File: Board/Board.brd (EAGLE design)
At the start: 72 x 50 mm, 19 parts

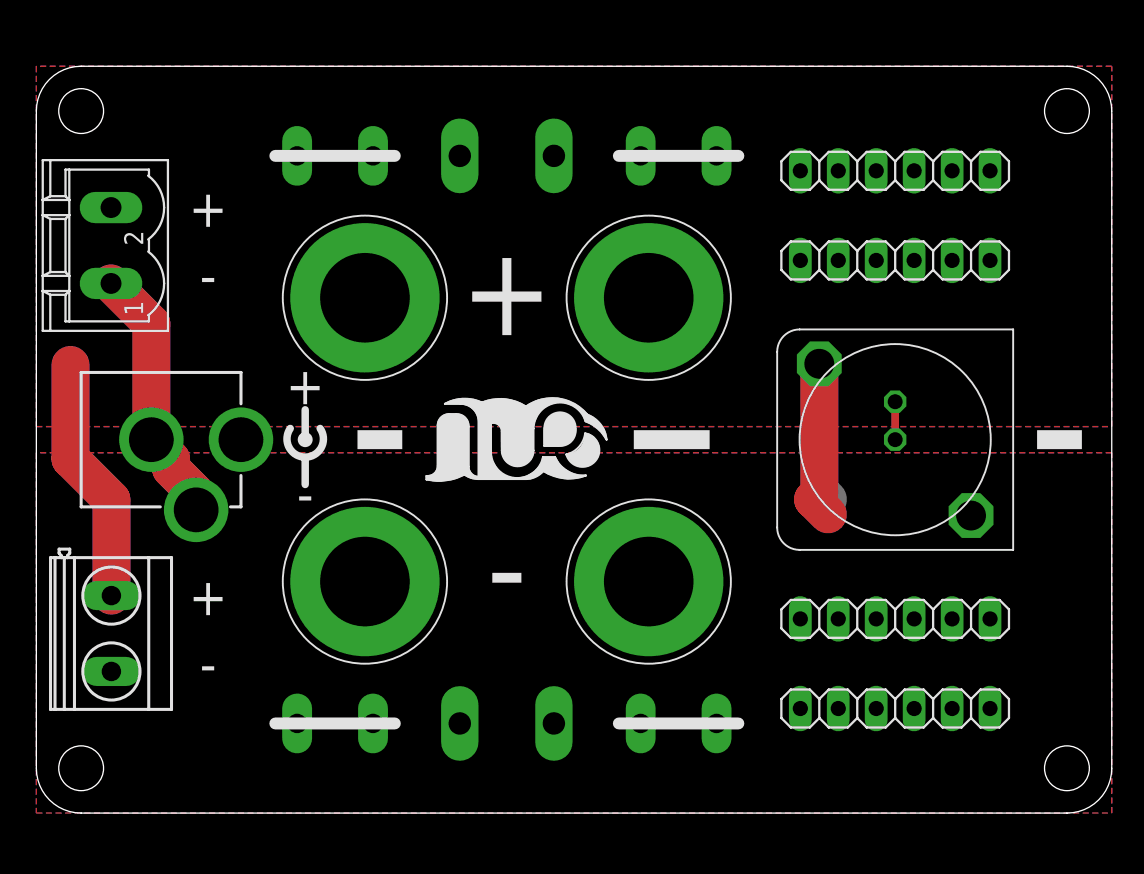
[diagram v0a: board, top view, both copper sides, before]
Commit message: moved BNC to center for better access to lower profile connectors
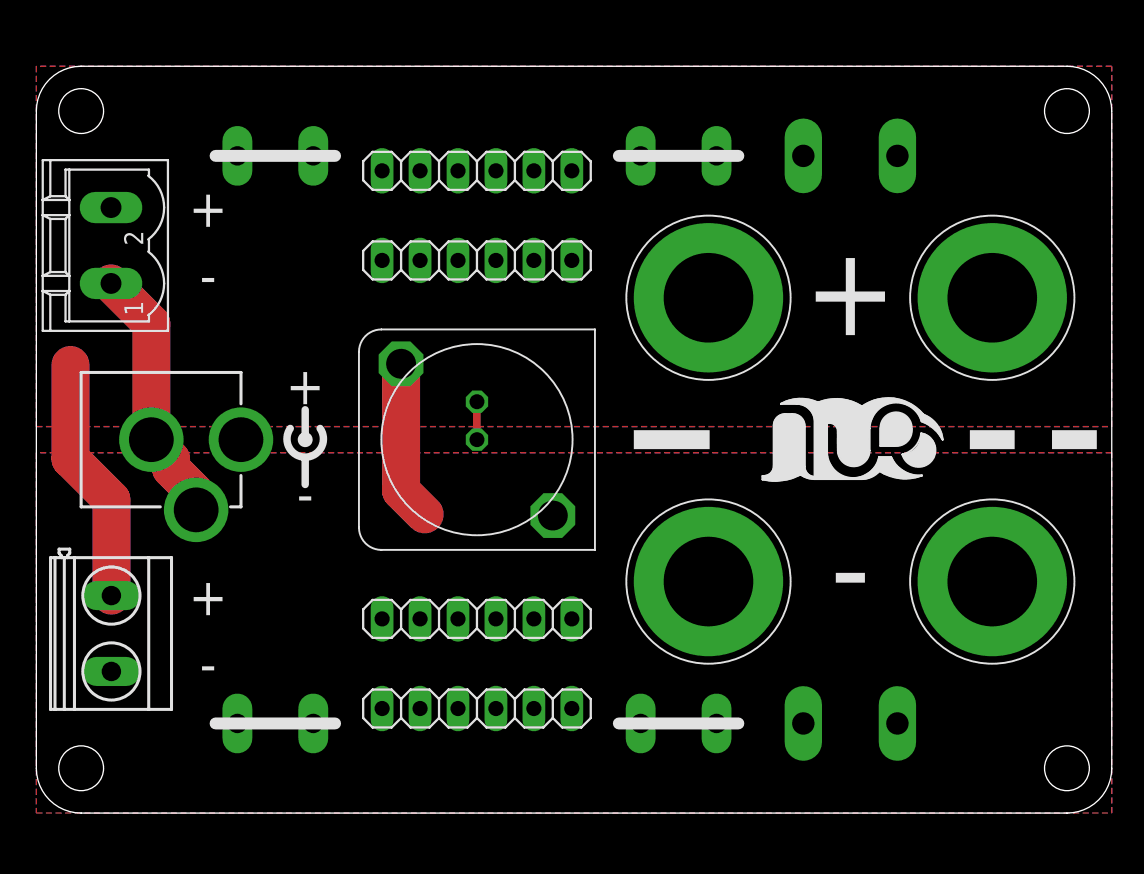
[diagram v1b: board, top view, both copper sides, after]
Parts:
- moved U$5 28.0 mm to (29.5, 25.0)
- moved U$6 28.0 mm to (29.5, 7.00)
- moved U$7 28.0 mm to (29.5, 43.0)
- moved U$8 28.0 mm to (29.5, 13.0)
- moved U$9 28.0 mm to (29.5, 37.0)
- moved U$18 27.0 mm to (16.0, 6.00), turned to 180 degrees
- moved U$19 27.0 mm to (16.0, 44.0), turned to 180 degrees
- moved U$1 23.0 mm to (64.0, 15.5), turned to 180 degrees
- moved U$14 23.0 mm to (43.0, 6.00), turned to 180 degrees
- moved U$15 23.0 mm to (43.0, 44.0), turned to 180 degrees
- moved U$16 23.0 mm to (54.5, 44.0)
- moved U$17 23.0 mm to (54.5, 6.00)
- moved U$2 23.0 mm to (45.0, 34.5), turned to 180 degrees
- moved U$3 23.0 mm to (45.0, 15.5), turned to 180 degrees
- moved U$4 23.0 mm to (64.0, 34.5), turned to 180 degrees
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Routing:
- net -: track 55.0 -> 56.5 mm

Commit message: implemented various suggestions from the forum post
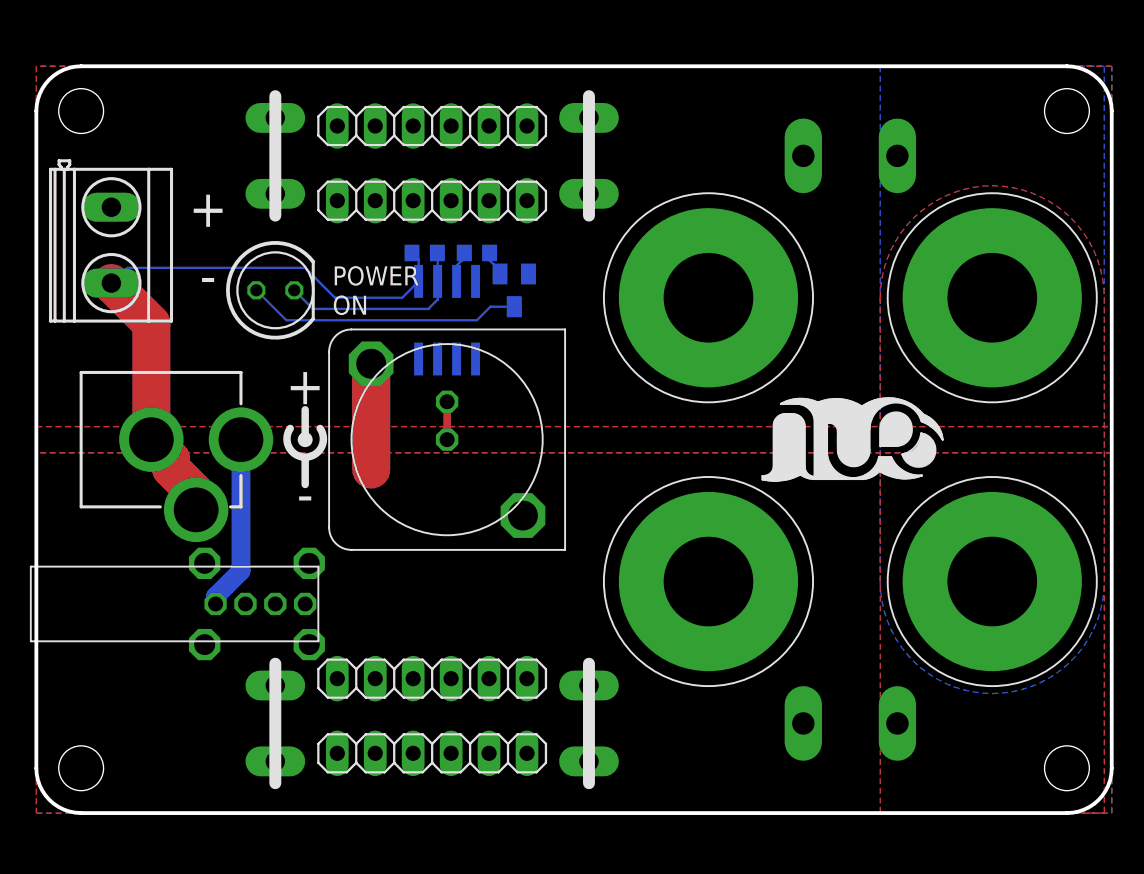
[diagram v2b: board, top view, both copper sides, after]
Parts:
- removed U$11: TERMINAL-BLOCK-2PLUG-IN, AdapterBoard:MSTBV2
- added IC1: LM334, linear:SO08
- added POWER: (no value), led:LED5MM
- added R1: 100, rcl:R0603
- added R2: 3R3, rcl:R0603
- added T1: BC807, transistor:SOT23-BEC
- added U$20: (no value), SparkFun-Aesthetics:OSHW-LOGO-L
- added U$21: USB, AdapterBoard:ECON-USBBUVA
- U$1, U$3: value 6MM-BANANA-PLUG -> 6MM-BANANA-PLUGSCREW-BLACK; device AdapterBoard:6MM-BANANA-MOUNT -> AdapterBoard:6MM-TERMINAL-POST-BLACK
- U$2, U$4: value 6MM-BANANA-PLUG -> 6MM-BANANA-PLUGSCREW-RED; device AdapterBoard:6MM-BANANA-MOUNT -> AdapterBoard:6MM-TERMINAL-POST-RED
- moved U$10 26.0 mm to (5.00, 38.0)
- moved U$1 19.0 mm to (64.0, 34.5)
- moved U$4 19.0 mm to (64.0, 15.5)
- moved U$14 6.00 mm to (37.0, 6.00), turned to 270 degrees
- moved U$15 6.00 mm to (37.0, 44.0), turned to 270 degrees
- moved U$8 5.00 mm to (26.5, 9.00)
- moved U$9 5.00 mm to (26.5, 41.0)
- moved U$6 4.24 mm to (26.5, 4.00)
- moved U$7 4.24 mm to (26.5, 46.0)
- moved U$5 2.00 mm to (27.5, 25.0)
- turned U$18 to 90 degrees
- turned U$19 to 90 degrees
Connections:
- removed net +: U$10.1, U$11.2, U$12.PWR, U$15.P$1, U$15.P$2, U$16.P$1, U$16.P$2, U$19.P$1, U$19.P$2, U$2.P$1, U$4.P$1, U$5.CONDUCTOR1, U$5.CONDUCTOR2, U$7.1, U$7.2, U$7.3, U$7.4, U$7.5, U$7.6, U$9.1, U$9.2, U$9.3, U$9.4, U$9.5, U$9.6
- removed net -: U$1.P$1, U$10.2, U$11.1, U$12.GND, U$12.GNDBREAK, U$14.P$1, U$14.P$2, U$17.P$1, U$17.P$2, U$18.P$1, U$18.P$2, U$3.P$1, U$5.SHIELD1, U$5.SHIELD2, U$6.1, U$6.2, U$6.3, U$6.4, U$6.5, U$6.6, U$8.1, U$8.2, U$8.3, U$8.4, U$8.5, U$8.6
- new net N$1: IC1.2, POWER.K, R2.2
- new net N$2: R1.2, T1.B
- new net N$3: IC1.3, R1.1
- new net N$4: POWER.A, T1.C
- new net V+: T1.E, U$10.1, U$12.PWR, U$15.P$1, U$15.P$2, U$16.P$1, U$16.P$2, U$19.P$1, U$19.P$2, U$2.P$1, U$21.V+, U$4.P$1, U$5.CONDUCTOR1, U$5.CONDUCTOR2, U$7.1, U$7.2, U$7.3, U$7.4, U$7.5, U$7.6, U$9.1, U$9.2, U$9.3, U$9.4, U$9.5, U$9.6
- new net V-: IC1.1, R2.1, U$1.P$1, U$10.2, U$12.GND, U$12.GNDBREAK, U$14.P$1, U$14.P$2, U$17.P$1, U$17.P$2, U$18.P$1, U$18.P$2, U$21.S1, U$21.S2, U$21.S3, U$21.S4, U$21.V-, U$3.P$1, U$5.SHIELD1, U$5.SHIELD2, U$6.1, U$6.2, U$6.3, U$6.4, U$6.5, U$6.6, U$8.1, U$8.2, U$8.3, U$8.4, U$8.5, U$8.6
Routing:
- net V-: track 0.00 -> 73.6 mm
- net -: track 56.5 -> 0.00 mm
- net +: track 35.7 -> 0.00 mm
- net N$4: track 0.00 -> 18.5 mm
- net V+: track 0.00 -> 14.2 mm
- net N$1: track 0.00 -> 13.5 mm
- net N$3: track 0.00 -> 2.11 mm
- net N$2: track 0.00 -> 1.69 mm
- added copper zone on layer 1, net V+
- added copper zone on layer 16, net V+
- added copper zone on layer 1, net V-
- added copper zone on layer 16, net V-
- removed copper zone on layer 1, net +
- removed copper zone on layer 16, net +
- removed copper zone on layer 1, net -
- removed copper zone on layer 16, net -
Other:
- board text added: "ON"
- board text added: "https://github.com/dangrie158/AdapterBox"

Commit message: fixed BNC pinout
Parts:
- removed U$20: (no value), SparkFun-Aesthetics:OSHW-LOGO-L
- turned U$5 to 90 degrees
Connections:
- net V+: no longer U$5.CONDUCTOR2
- net V-: now also U$5.CONDUCTOR2
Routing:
- net V+: track 14.2 -> 51.2 mm
- net V-: track 73.6 -> 94.5 mm

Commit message: updated BNC footprint
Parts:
- T1: device transistor:SOT23-BEC -> DC_LOAD_AU:SOT23-BEC
- U$5: value BNC-VTE-1-1337541-0 -> BNC-V; device AdapterBoard:BNC-V -> AdapterBoard:TE-5-1634503-1
- U$6, U$7: value PINHD-6 -> (none); device AdapterBoard:1X06 -> SparkFun-Connectors:1X06_LOCK_LONGPADS
- U$8, U$9: value PINHD-6FEMALE -> (none); device AdapterBoard:1X06F -> SparkFun-Connectors:1X06_LOCK_LONGPADS
- moved U$6 6.35 mm to (20.1, 4.00)
- moved U$7 6.35 mm to (20.1, 46.0)
- moved U$8 6.35 mm to (20.1, 9.00)
- moved U$9 6.35 mm to (20.1, 41.0)
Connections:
- net V+: now also U$5.C; no longer U$5.CONDUCTOR1
- net V-: now also U$5.S1, U$5.S2, U$5.S3, U$5.S4; no longer U$5.CONDUCTOR2, U$5.SHIELD1, U$5.SHIELD2
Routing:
- net V+: track 51.2 -> 25.8 mm
- net V-: track 94.5 -> 72.0 mm
- net N$2: track 1.69 -> 2.19 mm
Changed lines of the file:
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@@
 <element name="U$3" library="AdapterBoard" library_urn="urn:adsk.eagle:library:6658125" package="6MM-TERMINAL-POST-BLACK" package3d_urn="urn:adsk.eagle:package:6717096/2" value="6MM-BANANA-PLUGSCREW-BLACK" x="45" y="15.5" smashed="yes" rot="R180"/>
 <element name="U$4" library="AdapterBoard" library_urn="urn:adsk.eagle:library:6658125" package="6MM-TERMINAL-POST-RED" package3d_urn="urn:adsk.eagle:package:6717381/2" value="6MM-BANANA-PLUGSCREW-RED" x="64" y="15.5" smashed="yes" rot="R180"/>
-<element name="U$5" library="AdapterBoard" library_urn="urn:adsk.eagle:library:6658125" package="BNC-V" package3d_urn="urn:adsk.eagle:package:6658128/5" value="BNC-VTE-1-1337541-0" x="27.5" y="25" smashed="yes" rot="R90">
-<attribute name="MANUFACTURERNUMBER" value="TE-Connectivity 1-1337541-0" x="36.39" y="71.99" size="1.778" layer="27" rot="R90" display="off"/>
-</element>
-<element name="U$6" library="AdapterBoard" library_urn="urn:adsk.eagle:library:6658125" package="1X06" package3d_urn="urn:adsk.eagle:package:6665747/1" value="PINHD-6" x="26.5" y="4" smashed="yes"/>
-<element name="U$7" library="AdapterBoard" library_urn="urn:adsk.eagle:library:6658125" package="1X06" package3d_urn="urn:adsk.eagle:package:6665747/1" value="PINHD-6" x="26.5" y="46" smashed="yes"/>
-<element name="U$8" library="AdapterBoard" library_urn="urn:adsk.eagle:library:6658125" package="1X06F" package3d_urn="urn:adsk.eagle:package:6658229/3" value="PINHD-6FEMALE" x="26.5" y="9" smashed="yes"/>
-<element name="U$9" library="AdapterBoard" library_urn="urn:adsk.eagle:library:6658125" package="1X06F" package3d_urn="urn:adsk.eagle:package:6658229/3" value="PINHD-6FEMALE" x="26.5" y="41" smashed="yes"/>
+<element name="U$5" library="AdapterBoard" library_urn="urn:adsk.eagle:library:6658125" package="TE-5-1634503-1" package3d_urn="urn:adsk.eagle:package:7174046/2" value="BNC-V" x="27.5" y="25" smashed="yes" rot="R90"/>
+<element name="U$6" library="SparkFun-Connectors" library_urn="urn:adsk.eagle:library:513" package="1X06_LOCK_LONGPADS" package3d_urn="urn:adsk.eagle:package:38121/1" value="" x="20.15" y="4" smashed="yes"/>
+<element name="U$7" library="SparkFun-Connectors" library_urn="urn:adsk.eagle:library:513" package="1X06_LOCK_LONGPADS" package3d_urn="urn:adsk.eagle:package:38121/1" value="" x="20.15" y="46" smashed="yes"/>
+<element name="U$8" library="SparkFun-Connectors" library_urn="urn:adsk.eagle:library:513" package="1X06_LOCK_LONGPADS" package3d_urn="urn:adsk.eagle:package:38121/1" value="" x="20.15" y="9" smashed="yes"/>
+<element name="U$9" library="SparkFun-Connectors" library_urn="urn:adsk.eagle:library:513" package="1X06_LOCK_LONGPADS" package3d_urn="urn:adsk.eagle:package:38121/1" value="" x="20.15" y="41" smashed="yes"/>
 <element name="U$13" library="AdapterBoard" library_urn="urn:adsk.eagle:library:6658125" package="LOGO-SILKSCREEN" package3d_urn="urn:adsk.eagle:package:6663173/1" value="" x="54.5" y="24" smashed="yes"/>
 <element name="U$14" library="AdapterBoard" library_urn="urn:adsk.eagle:library:6658125" package="TE-726386" package3d_urn="urn:adsk.eagle:package:6665093/5" value="TERMINAL-1" x="37" y="6" smashed="yes" rot="R270"/>
@@
 <attribute name="VALUE" x="19.2004" y="33.1966" size="1.27" layer="27" ratio="10"/>
 </element>
-<element name="T1" library="transistor" library_urn="urn:adsk.eagle:library:402" package="SOT23-BEC" package3d_urn="urn:adsk.eagle:package:29919/2" value="BC807" x="32" y="35" smashed="yes" rot="MR180">
+<element name="T1" library="DC_LOAD_AU" library_urn="urn:adsk.eagle:library:220454" package="SOT23-BEC" package3d_urn="urn:adsk.eagle:package:220536/2" value="BC807" x="32" y="35" smashed="yes" rot="MR180">
 <attribute name="VALUE" x="32" y="32.427" size="0.8128" layer="26" rot="MR180" align="center"/>
 </element>
@@
 <contactref element="R1" pad="2"/>
 <wire x1="30.35" y1="37.5" x2="30.35" y2="37" width="0.1524" layer="16"/>
-<wire x1="30.35" y1="37" x2="31.05" y2="36.3" width="0.1524" layer="16"/>
-<wire x1="31.05" y1="36.3" x2="31.05" y2="36.1" width="0.1524" layer="16"/>
+<wire x1="30.35" y1="37.5" x2="31.05" y2="36.8" width="0.1524" layer="16"/>
+<wire x1="31.05" y1="36.8" x2="31.05" y2="36.1" width="0.1524" layer="16"/>
 </signal>
 <signal name="N$3">
@@
 <contactref element="T1" pad="C"/>
 <contactref element="POWER" pad="A"/>
-<wire x1="32" y1="33.9" x2="30.4" y2="33.9" width="0.1524" layer="16"/>
-<wire x1="30.4" y1="33.9" x2="29.5" y2="33" width="0.1524" layer="16"/>
-<wire x1="29.5" y1="33" x2="16.73" y2="33" width="0.1524" layer="16"/>
 <wire x1="16.73" y1="33" x2="14.73" y2="35" width="0.1524" layer="16"/>
+<wire x1="32" y1="33.9" x2="30.48" y2="33.9" width="0.1524" layer="16"/>
+<wire x1="30.48" y1="33.9" x2="29.58" y2="33" width="0.1524" layer="16"/>
+<wire x1="29.58" y1="33" x2="16.73" y2="33" width="0.1524" layer="16"/>
 </signal>
 <signal name="V+">
 <contactref element="U$2" pad="P$1"/>
-<contactref element="U$5" pad="CONDUCTOR1"/>
+<contactref element="U$5" pad="C"/>
 <contactref element="U$4" pad="P$1"/>
 <contactref element="U$7" pad="1"/>
@@
 <wire x1="13.7" y1="16.2" x2="12" y2="14.5" width="1.27" layer="16"/>
 <wire x1="12" y1="14" x2="12" y2="14.5" width="1.27" layer="16"/>
-<wire x1="27.77" y1="41" x2="27.8233375" y2="38.09785625" width="0.8128" layer="1"/>
-<wire x1="27.5" y1="25" x2="27.5" y2="37.77451875" width="0.8128" layer="1"/>
-<wire x1="27.5" y1="37.77451875" x2="27.8233375" y2="38.09785625" width="0.8128" layer="1"/>
 <wire x1="27.5" y1="25" x2="27.5" y2="27.5" width="0.8128" layer="16"/>
 <wire x1="27.5" y1="27.5" x2="27.94" y2="27.94" width="0.8128" layer="16"/>
-<wire x1="27.94" y1="27.94" x2="33.02" y2="27.94" width="0.8128" layer="16"/>
-<wire x1="36.83" y1="38.1" x2="36.83" y2="31.75" width="0.8128" layer="16"/>
-<wire x1="33.02" y1="27.94" x2="36.83" y2="31.75" width="0.8128" layer="16"/>
-<wire x1="37" y1="41.46" x2="37" y2="38.27" width="0.8128" layer="16"/>
-<wire x1="37" y1="38.27" x2="36.83" y2="38.1" width="0.8128" layer="16"/>
+<wire x1="32.95" y1="36.1" x2="32.95" y2="40.646" width="0.1524" layer="16"/>
+<wire x1="32.95" y1="40.646" x2="32.85" y2="40.746" width="0.1524" layer="16"/>
+<wire x1="27.5" y1="25" x2="27.5" y2="26.23" width="0.8128" layer="1"/>
+<wire x1="27.5" y1="26.23" x2="27.94" y2="26.67" width="0.8128" layer="1"/>
+<wire x1="27.5" y1="25" x2="27.5" y2="28.77" width="0.8128" layer="1"/>
+<wire x1="27.5" y1="28.77" x2="27.94" y2="29.21" width="0.8128" layer="1"/>
 </signal>
 <signal name="V-">
@@
 <contactref element="U$8" pad="1"/>
 <contactref element="U$1" pad="P$1"/>
-<contactref element="U$5" pad="SHIELD1" route="any" routetag="G$1.S"/>
-<contactref element="U$5" pad="SHIELD2" route="any" routetag="G$1.S"/>
+<contactref element="U$5" pad="S2"/>
+<contactref element="U$5" pad="S3"/>
 <contactref element="U$3" pad="P$1"/>
 <contactref element="U$6" pad="1"/>
@@
 <wire x1="20" y1="34.5" x2="18" y2="36.5" width="0.1524" layer="16"/>
 <wire x1="18" y1="36.5" x2="6.09" y2="36.5" width="0.1524" layer="16"/>
-<wire x1="22.42" y1="23" x2="18.27" y2="23" width="0.8128" layer="1"/>
-<wire x1="18.27" y1="23" x2="18.27" y2="16.72" width="0.8128" layer="1"/>
-<wire x1="22.42" y1="23" x2="18.27" y2="23" width="0.8128" layer="16"/>
-<wire x1="18.27" y1="23" x2="18.27" y2="16.72" width="0.8128" layer="16"/>
-<contactref element="U$5" pad="CONDUCTOR2" route="any" routetag="G$1.S"/>
-<wire x1="22.42" y1="30.08" x2="22.42" y2="23" width="2.54" layer="1"/>
-<wire x1="22.42" y1="30.08" x2="22.42" y2="23" width="2.54" layer="16"/>
+<contactref element="U$5" pad="S1"/>
+<contactref element="U$5" pad="S4"/>
+<wire x1="30.63" y1="28.13" x2="30.63" y2="21.87" width="0.8128" layer="16"/>
+<wire x1="24.37" y1="28.13" x2="24.37" y2="21.87" width="0.8128" layer="16"/>
 </signal>
 </signals>

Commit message: updated pinheader 3d models
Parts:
- U$6, U$7: value (none) -> PINHEADER-1X6MALE_LOCK; device SparkFun-Connectors:1X06_LOCK_LONGPADS -> AdapterBoard:1X06_LOCK
- U$8, U$9: value (none) -> PINHEADER-1X6FEMALE_LOCK; device SparkFun-Connectors:1X06_LOCK_LONGPADS -> AdapterBoard:1X06_FEMALE_LOCK.010
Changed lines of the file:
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@@
 <drawing>
 <settings>
-<setting alwaysvectorfont="no"/>
+<setting alwaysvectorfont="yes"/>
 <setting verticaltext="up"/>
 </settings>
@@
 </layers>
 <board>
-<fusionsync huburn="a.cGVyc29uYWw6dWUyOWFjMzc0" projecturn="a.cGVyc29uYWw6dWUyOWFjMzc0IzIwMTgxMTA5MTU5MzcxODUx" f3durn="urn:adsk.wipprod:dm.lineage:8R8TAl3XTbGenGFVYcsrqQ" pcbguid="c32a4f4f-8cd4-4b95-b40a-19347d32ef6f" lastpulledtime="2018-11-11T17:12:34Z" lastsyncedchangeguid="75f5500a-d46a-adba-61ab-fc7971ac2392"/>
+<fusionsync huburn="a.cGVyc29uYWw6dWUyOWFjMzc0" projecturn="a.cGVyc29uYWw6dWUyOWFjMzc0IzIwMTgxMTA5MTU5MzcxODUx" f3durn="urn:adsk.wipprod:dm.lineage:8R8TAl3XTbGenGFVYcsrqQ" pcbguid="c32a4f4f-8cd4-4b95-b40a-19347d32ef6f" lastpulledtime="2018-11-11T17:12:34Z" lastsyncedchangeguid="f148739b-0e27-b40c-a1d0-ee1bb420b8f3"/>
 <plain>
 <text x="11.5" y="40.5" size="2.5" layer="21" font="fixed" align="center">+</text>
@@
 <element name="U$4" library="AdapterBoard" library_urn="urn:adsk.eagle:library:6658125" package="6MM-TERMINAL-POST-RED" package3d_urn="urn:adsk.eagle:package:6717381/2" value="6MM-BANANA-PLUGSCREW-RED" x="64" y="15.5" smashed="yes" rot="R180"/>
 <element name="U$5" library="AdapterBoard" library_urn="urn:adsk.eagle:library:6658125" package="TE-5-1634503-1" package3d_urn="urn:adsk.eagle:package:7174046/2" value="BNC-V" x="27.5" y="25" smashed="yes" rot="R90"/>
-<element name="U$6" library="SparkFun-Connectors" library_urn="urn:adsk.eagle:library:513" package="1X06_LOCK_LONGPADS" package3d_urn="urn:adsk.eagle:package:38121/1" value="" x="20.15" y="4" smashed="yes"/>
-<element name="U$7" library="SparkFun-Connectors" library_urn="urn:adsk.eagle:library:513" package="1X06_LOCK_LONGPADS" package3d_urn="urn:adsk.eagle:package:38121/1" value="" x="20.15" y="46" smashed="yes"/>
-<element name="U$8" library="SparkFun-Connectors" library_urn="urn:adsk.eagle:library:513" package="1X06_LOCK_LONGPADS" package3d_urn="urn:adsk.eagle:package:38121/1" value="" x="20.15" y="9" smashed="yes"/>
-<element name="U$9" library="SparkFun-Connectors" library_urn="urn:adsk.eagle:library:513" package="1X06_LOCK_LONGPADS" package3d_urn="urn:adsk.eagle:package:38121/1" value="" x="20.15" y="41" smashed="yes"/>
+<element name="U$6" library="AdapterBoard" library_urn="urn:adsk.eagle:library:6658125" package="1X06_LOCK" package3d_urn="urn:adsk.eagle:package:7198025/2" value="PINHEADER-1X6MALE_LOCK" x="20.15" y="4" smashed="yes"/>
+<element name="U$7" library="AdapterBoard" library_urn="urn:adsk.eagle:library:6658125" package="1X06_LOCK" package3d_urn="urn:adsk.eagle:package:7198025/2" value="PINHEADER-1X6MALE_LOCK" x="20.15" y="46" smashed="yes"/>
+<element name="U$8" library="AdapterBoard" library_urn="urn:adsk.eagle:library:6658125" package="1X06_FEMALE_LOCK.010" package3d_urn="urn:adsk.eagle:package:7198026/2" value="PINHEADER-1X6FEMALE_LOCK" x="20.15" y="9" smashed="yes"/>
+<element name="U$9" library="AdapterBoard" library_urn="urn:adsk.eagle:library:6658125" package="1X06_FEMALE_LOCK.010" package3d_urn="urn:adsk.eagle:package:7198026/2" value="PINHEADER-1X6FEMALE_LOCK" x="20.15" y="41" smashed="yes"/>
 <element name="U$13" library="AdapterBoard" library_urn="urn:adsk.eagle:library:6658125" package="LOGO-SILKSCREEN" package3d_urn="urn:adsk.eagle:package:6663173/1" value="" x="54.5" y="24" smashed="yes"/>
 <element name="U$14" library="AdapterBoard" library_urn="urn:adsk.eagle:library:6658125" package="TE-726386" package3d_urn="urn:adsk.eagle:package:6665093/5" value="TERMINAL-1" x="37" y="6" smashed="yes" rot="R270"/>
